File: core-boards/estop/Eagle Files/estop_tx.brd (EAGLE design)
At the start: 76.2 x 50.8 mm, 29 parts, among them J1 RFM95W-3072, J2 JST-XH-02-PIN-ROUND-PAD, J3 JST-XH-02-PIN-ROUND-PAD, J4 JST-XH-02-PIN-ROUND-PAD, J5 JST-XH-02-PIN-ROUND-PAD, J6 B2PS-VH(LF)(SN), U1 R-78E5.0-1.0CONV_R-78E5.0-1.0, U2 TXB0106PWR, U4 ATMEGA328P-AUR

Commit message: estop tx design review
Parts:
- added D4: Green, SparkFun-LED:LED-0603
- added R7: 10k, rcl:R0603
- added U$1: (no value), RoboJackets-Aesthetics:ROBOBUZZ_1.0X
- C6: device resistor:C0603 -> rcl:C0603
- R2: value 10k -> 1k
- R3: value 60k -> 10k
- R4, R5, R6: device resistor:R0603 -> rcl:R0603
- moved R3 46.2 mm to (53.0, 38.0), turned to 90 degrees
- moved R2 33.1 mm to (39.0, 7.00), turned to 180 degrees
- moved J5 29.5 mm to (31.6, 2.58), turned to 0 degrees
- moved J4 24.9 mm to (21.5, 2.63), turned to 0 degrees
- moved C5 10.4 mm to (20.9, 22.1), turned to 90 degrees
- moved C8 10.0 mm to (20.4, 8.47), turned to 270 degrees
- moved R4 2.30 mm to (39.0, 11.0), turned to 180 degrees
- moved J3 2.24 mm to (11.2, 2.56)
- moved D1 2.22 mm to (44.0, 11.0)
- moved R6 1.91 mm to (39.0, 15.0), turned to 180 degrees
- moved C4 1.89 mm to (59.0, 34.0)
- moved D3 1.82 mm to (44.0, 15.0)
- moved R5 1.68 mm to (39.0, 19.0), turned to 180 degrees
- moved D2 1.58 mm to (44.0, 19.0)
- moved C3 1.46 mm to (45.0, 30.0), turned to 90 degrees
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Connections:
- new net BUTTON_LED_CONN: J5.1, U2.3
- new net N$5: D4.C, R2.1
- new net WIRELESS_LED_CONN: J4.1, U2.1
- net !RESET: now also R3.2; no longer R2.1
- net +3V3: now also D4.A, U2.8
- net +5V: now also D1.A, R3.1; no longer D2.A, R2.2
- net BUTTON_LED: now also D3.A; no longer D1.A, J5.1, U2.3
- net CE: now also U4.14; no longer U4.7
- net GND: now also R2.2, R4.2, R5.2, R6.2, R7.2; no longer J1.9, R3.1, R4.1, R5.1, R6.1
- net N$2: now also D1.C, R4.1; no longer D2.C, R5.2
- net N$3: now also D3.C, R6.1; no longer D1.C, R4.2
- net N$4: now also D2.C, R5.1; no longer D3.C, R6.2
- net N$6: now also J1.9, R7.1; no longer R3.2, U2.8
- net WIRELESS_LED: now also D2.A; no longer D3.A, J4.1, U2.1
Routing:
- net BUTTON_LED: track 62.3 -> 43.8 mm, vias 6 -> 4
- net WIRELESS_LED: track 58.2 -> 41.2 mm
- net BUTTON_LED_CONN: track 0.00 -> 14.4 mm
- net CE: track 32.1 -> 44.7 mm
- net WIRELESS_LED_CONN: track 0.00 -> 10.6 mm
- net MISO: track 69.7 -> 64.3 mm, vias 4 -> 0
- net SCK: track 71.1 -> 67.3 mm
- net +5V: track 0.00 -> 3.42 mm
- net +3V3: track 0.00 -> 3.28 mm
- net N$5: track 0.00 -> 3.27 mm
- net MOSI: track 69.4 -> 66.2 mm, vias 0 -> 2
- net GND: track 54.6 -> 56.7 mm, vias 22 -> 23
- net N$9: track 2.47 -> 4.50 mm
- net !RESET: track 39.3 -> 37.5 mm
- net N$6: track 3.43 -> 4.53 mm
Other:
- board text added: "3V3"
- board text added: "5V"
- board text added: "BUTTON"
- board text added: "BUTTON IN"
- board text added: "E-Stop Board TX"
- board text added: "POWER"
- board text added: "POWER IN"
- board text added: "RoboJackets IGVC"
- board text added: "WIRELESS"
- board text added: "v1.2"

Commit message: almost order ready haha
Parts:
- removed J2: JST-XH-02-PIN-ROUND-PAD, IGVC-Connector:JST-XH-02-PACKAGE-ROUND-PAD
- added J7: 2-PIN_2MM-V, RoboJackets-Connectors:2MM-2-V
- added R10, R8, R9: 200, rcl:R0603
- added R11: 10k, rcl:R0603
- J3, J4, J5: value JST-XH-02-PIN-ROUND-PAD -> 2-PIN_2MM-V; device IGVC-Connector:JST-XH-02-PACKAGE-ROUND-PAD -> RoboJackets-Connectors:2MM-2-V
- moved C7 10.5 mm to (64.2, 21.7), turned to 90 degrees
- moved R1 6.30 mm to (58.5, 7.66), turned to 180 degrees
- moved J3 1.11 mm to (11.4, 3.65)
- moved J5 1.07 mm to (31.7, 3.65)
- moved J4 1.03 mm to (21.5, 3.66)
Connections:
- new net N$1: J3.1, R8.1
- new net N$10: J1.3, R11.1
- new net N$7: J4.1, R9.1
- new net N$8: J5.1, R10.1
- net +3V3: now also R8.2; no longer J3.1
- net +5V: now also R11.2
- net BUTTON_LED_CONN: now also R10.2; no longer J5.1
- net GND: now also J7.2, U2.10, U2.11, U2.12, U2.13, U2.4, U2.5, U2.6, U2.7; no longer J2.2
- net IN: now also J7.1; no longer J2.1
- net WIRELESS_LED_CONN: now also R9.2; no longer J4.1
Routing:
- net GND: track 56.7 -> 73.1 mm, vias 23 -> 24
- net BUTTON_LED_CONN: track 14.4 -> 5.13 mm
- net N$8: track 0.00 -> 8.10 mm
- net WIRELESS_LED_CONN: track 10.6 -> 3.45 mm
- net N$1: track 0.00 -> 6.08 mm
- net N$7: track 0.00 -> 5.08 mm
- net N$10: track 0.00 -> 3.97 mm
- net IN: track 27.9 -> 29.6 mm
- net WIRELESS_LED: track 41.2 -> 40.6 mm
- net BUTTON_LED: track 43.8 -> 43.2 mm

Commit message: things should be done tm
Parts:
- C1, C7: device rcl:C0603 -> rcl:C0805
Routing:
- net GND: track 73.1 -> 74.1 mm
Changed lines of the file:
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@@
 <attribute name="VALUE" x="75.946" y="14.224" size="1.27" layer="27" rot="R90" align="top-left"/>
 </element>
-<element name="C1" library="rcl" library_urn="urn:adsk.eagle:library:334" package="C0603" package3d_urn="urn:adsk.eagle:package:23616/2" value="10uF" x="65.405" y="10.922" smashed="yes" rot="R90">
+<element name="C1" library="rcl" library_urn="urn:adsk.eagle:library:334" package="C0805" package3d_urn="urn:adsk.eagle:package:23617/2" value="10uF" x="65.405" y="10.922" smashed="yes" rot="R90">
 <attribute name="NAME" x="64.77" y="10.287" size="0.5" layer="25" rot="R90"/>
-<attribute name="POPULARITY" value="37" x="65.405" y="10.922" size="1.778" layer="27" rot="R90" display="off"/>
+<attribute name="POPULARITY" value="63" x="65.405" y="10.922" size="1.778" layer="27" rot="R90" display="off"/>
 <attribute name="SPICEPREFIX" value="C" x="65.405" y="10.922" size="1.778" layer="27" rot="R90" display="off"/>
 <attribute name="VALUE" x="67.31" y="10.287" size="1.27" layer="27" rot="R90"/>
 </element>
-<element name="C7" library="rcl" library_urn="urn:adsk.eagle:library:334" package="C0603" package3d_urn="urn:adsk.eagle:package:23616/2" value="10uF" x="64.187" y="21.66" smashed="yes" rot="R90">
+<element name="C7" library="rcl" library_urn="urn:adsk.eagle:library:334" package="C0805" package3d_urn="urn:adsk.eagle:package:23617/2" value="10uF" x="64.187" y="21.66" smashed="yes" rot="R90">
 <attribute name="NAME" x="63.552" y="21.025" size="0.5" layer="25" rot="R90"/>
-<attribute name="POPULARITY" value="37" x="64.187" y="21.66" size="1.778" layer="27" rot="R90" display="off"/>
+<attribute name="POPULARITY" value="63" x="64.187" y="21.66" size="1.778" layer="27" rot="R90" display="off"/>
 <attribute name="SPICEPREFIX" value="C" x="64.187" y="21.66" size="1.778" layer="27" rot="R90" display="off"/>
 <attribute name="VALUE" x="66.092" y="21.025" size="1.27" layer="27" rot="R90"/>
@@
 </element>
 <element name="R11" library="rcl" library_urn="urn:adsk.eagle:library:334" package="R0603" package3d_urn="urn:adsk.eagle:package:23555/3" value="10k" x="31.65" y="31.27" smashed="yes" rot="R270">
-<attribute name="NAME" x="32.285" y="31.905" size="1.27" layer="25" rot="R270"/>
+<attribute name="NAME" x="32.285" y="31.905" size="0.5" layer="25" rot="R270"/>
 <attribute name="POPULARITY" value="77" x="31.65" y="31.27" size="1.778" layer="27" rot="R270" display="off"/>
 <attribute name="SPICEPREFIX" value="R" x="31.65" y="31.27" size="1.778" layer="27" rot="R270" display="off"/>
@@
 <wire x1="73.227" y1="9.227" x2="74" y2="10" width="0.4064" layer="1"/>
 <via x="74" y="10" extent="1-16" drill="0.35"/>
-<wire x1="65.405" y1="11.772" x2="65.633" y2="12" width="0.4064" layer="1"/>
-<wire x1="65.633" y1="12" x2="67" y2="12" width="0.4064" layer="1"/>
-<via x="67" y="12" extent="1-16" drill="0.35"/>
 <wire x1="73.116" y1="19.939" x2="71.061" y2="19.939" width="0.4064" layer="1"/>
 <wire x1="71.061" y1="19.939" x2="71" y2="20" width="0.4064" layer="1"/>
@@
 <wire x1="58.209" y1="44.209" x2="58" y2="44" width="0.4064" layer="1"/>
 <via x="58" y="44" extent="1-16" drill="0.35"/>
-<wire x1="64.187" y1="23.6188" x2="63.8058" y2="24" width="0.4064" layer="1"/>
-<wire x1="64.187" y1="23.6188" x2="64.187" y2="22.51" width="0.4064" layer="1"/>
-<via x="63.8058" y="24" extent="1-16" drill="0.35"/>
 <wire x1="50.752" y1="48.006" x2="52.006" y2="48.006" width="0.4064" layer="1"/>
 <wire x1="52.006" y1="48.006" x2="53" y2="49" width="0.4064" layer="1"/>
@@
 <wire x1="23.434996875" y1="12.4906" x2="23.434996875" y2="13.350003125" width="0.254" layer="1"/>
 <wire x1="23.434996875" y1="13.350003125" x2="22.785" y2="14" width="0.254" layer="1"/>
+<wire x1="65.405" y1="11.872" x2="66.128" y2="11.872" width="0.4064" layer="1"/>
+<wire x1="66.128" y1="11.872" x2="67" y2="11" width="0.4064" layer="1"/>
+<via x="67" y="11" extent="1-16" drill="0.35"/>
+<wire x1="64.187" y1="22.61" x2="62.61" y2="22.61" width="0.4064" layer="1"/>
+<wire x1="62.61" y1="22.61" x2="62" y2="22" width="0.4064" layer="1"/>
+<via x="62" y="22" extent="1-16" drill="0.35"/>
 </signal>
 <signal name="MISO">

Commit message: the ordered board :party-parrot
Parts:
- moved C8 0.22 mm to (20.6, 8.68)
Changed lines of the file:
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@@
 <attribute name="VALUE" x="22.815" y="21.461" size="1.27" layer="27" rot="R90"/>
 </element>
-<element name="C8" library="rcl" library_urn="urn:adsk.eagle:library:334" package="C0603" package3d_urn="urn:adsk.eagle:package:23616/2" value=".1uF" x="20.45" y="8.475" smashed="yes" rot="R270">
-<attribute name="NAME" x="21.085" y="9.11" size="0.5" layer="25" rot="R270"/>
-<attribute name="POPULARITY" value="37" x="20.45" y="8.475" size="1.778" layer="27" rot="R270" display="off"/>
-<attribute name="SPICEPREFIX" value="C" x="20.45" y="8.475" size="1.778" layer="27" rot="R270" display="off"/>
-<attribute name="VALUE" x="18.545" y="9.11" size="1.27" layer="27" rot="R270"/>
+<element name="C8" library="rcl" library_urn="urn:adsk.eagle:library:334" package="C0603" package3d_urn="urn:adsk.eagle:package:23616/2" value=".1uF" x="20.55" y="8.675" smashed="yes" rot="R270">
+<attribute name="NAME" x="21.185" y="9.31" size="0.5" layer="25" rot="R270"/>
+<attribute name="POPULARITY" value="37" x="20.55" y="8.675" size="1.778" layer="27" rot="R270" display="off"/>
+<attribute name="SPICEPREFIX" value="C" x="20.55" y="8.675" size="1.778" layer="27" rot="R270" display="off"/>
+<attribute name="VALUE" x="18.645" y="9.31" size="1.27" layer="27" rot="R270"/>
 </element>
 <element name="J6" library="RoboJackets-Connectors" package="B2PS-CENTERED" value="B2PS-VH(LF)(SN)" x="71.247" y="7.747" smashed="yes">
@@
 <wire x1="38.15" y1="5.15" x2="38" y2="5" width="0.4064" layer="1"/>
 <via x="38" y="5" extent="1-16" drill="0.35"/>
-<wire x1="20.45" y1="7.625" x2="21.375" y2="7.625" width="0.4064" layer="1"/>
-<wire x1="21.375" y1="7.625" x2="22" y2="7" width="0.4064" layer="1"/>
-<via x="22" y="7" extent="1-16" drill="0.35"/>
+<wire x1="20.55" y1="7.825" x2="21.825" y2="7.825" width="0.4064" layer="1"/>
+<wire x1="21.825" y1="7.825" x2="22" y2="8" width="0.4064" layer="1"/>
+<via x="22" y="8" extent="1-16" drill="0.35"/>
 <wire x1="45" y1="30.85" x2="45" y2="31.026" width="0.4064" layer="1"/>
 <wire x1="45" y1="31.026" x2="47.7335" y2="31.026" width="0.4064" layer="1"/>
@@
 <vertex x="0.21" y="0.13"/>
 </polygon>
-<wire x1="20.185" y1="12.4906" x2="20.185" y2="9.59" width="0.4064" layer="1"/>
-<wire x1="20.185" y1="9.59" x2="20.45" y2="9.325" width="0.4064" layer="1"/>
+<wire x1="20.185" y1="12.4906" x2="20.185" y2="9.89" width="0.4064" layer="1"/>
+<wire x1="20.185" y1="9.89" x2="20.55" y2="9.525" width="0.4064" layer="1"/>
 <contactref element="R8" pad="2"/>
 </signal>

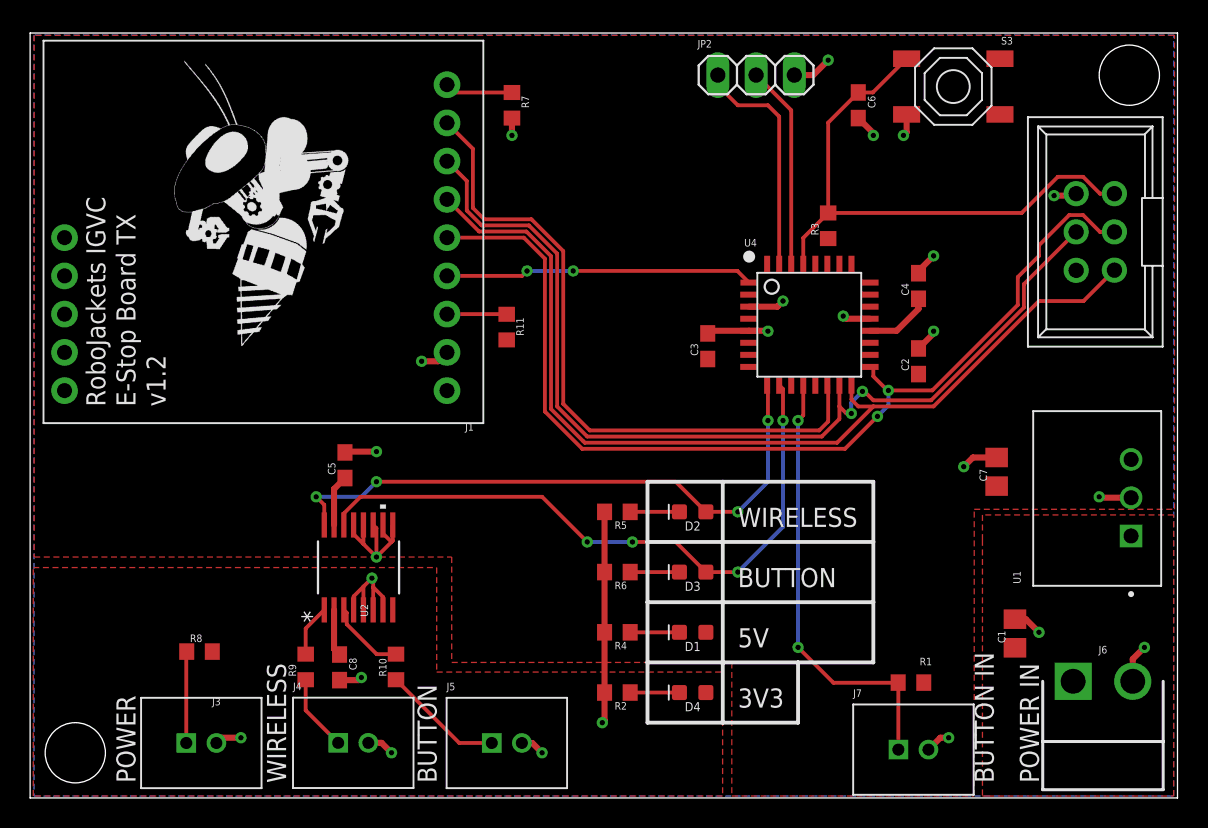
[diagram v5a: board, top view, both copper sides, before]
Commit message: Fixed estop-tx
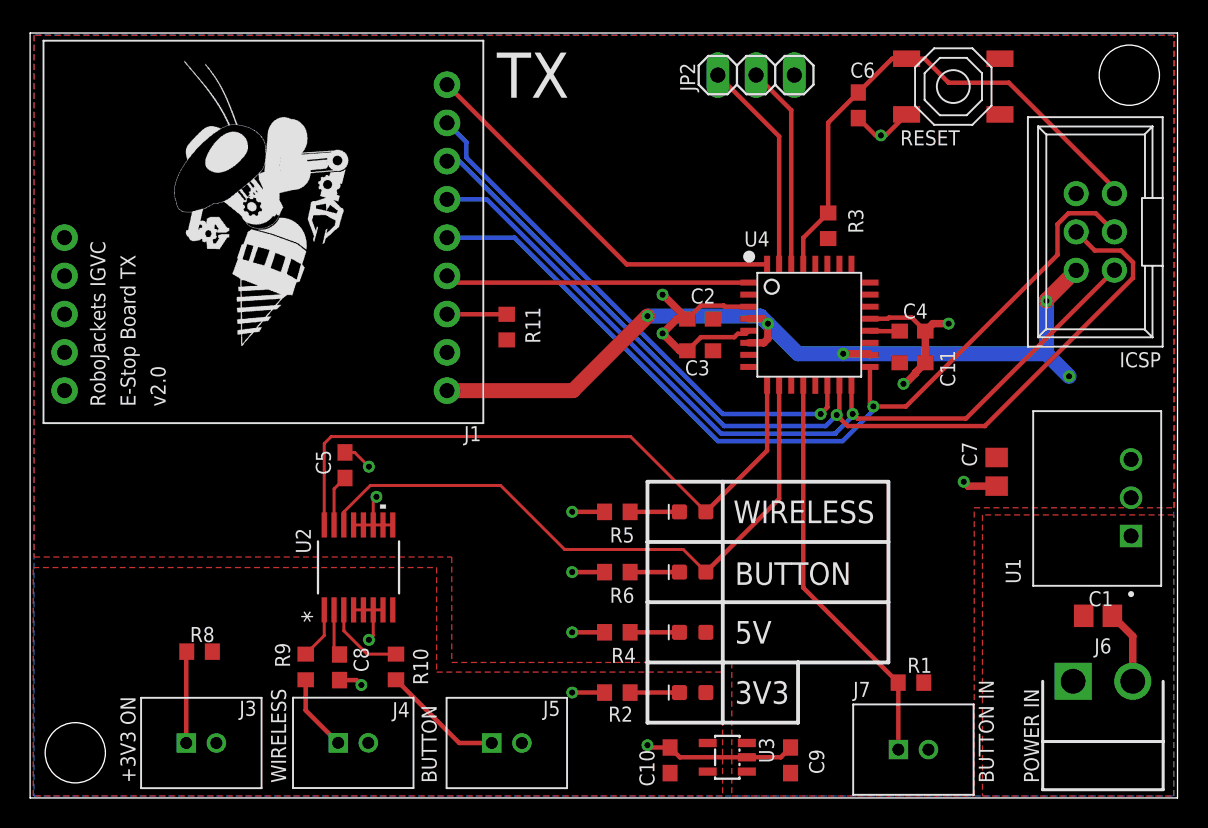
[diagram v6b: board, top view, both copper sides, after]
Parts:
- removed R7: 10k, rcl:R0603
- added C10, C9: 1uF, rcl:C0603
- added C11: 0.1uF, rcl:C0603
- added U3: MIC550X, IGVC-Regulator:SOT23-DBV
- moved C2 14.8 mm to (44.5, 31.8), turned to 180 degrees
- moved C1 5.64 mm to (70.9, 12.1), turned to 0 degrees
- moved C4 3.03 mm to (58.6, 31.0), turned to 0 degrees
- moved C3 0.58 mm to (44.5, 29.7), turned to 180 degrees
- turned C7 to 270 degrees
- renumbered PROG to ICSP, S3 to RESET
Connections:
- net IN renamed BUTTON-IN
- net N$10 renamed EN
- removed net N$6: J1.9, R7.1
- new net RADIO_RST: J1.9, U4.32
- net +3V3: now also C10.1, U3.5
- net +5V: now also C11.1, C9.1, U3.1, U3.3
- net GND: now also C10.2, C11.2, C9.2, U3.2; no longer R7.2
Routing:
- net +5V: track 3.42 -> 60.4 mm, vias 0 -> 5
- net RADIO_RST: track 0.00 -> 26.2 mm
- net CE: track 44.7 -> 35.5 mm, vias 0 -> 1
- net MISO: track 64.3 -> 57.5 mm, vias 0 -> 1
- net SCK: track 67.3 -> 60.8 mm, vias 2 -> 1
- net GND: track 73.8 -> 68.0 mm, vias 24 -> 15
- net N$6: track 4.53 -> 0.00 mm
- net BUTTON-IN: track 29.6 -> 26.8 mm, vias 2 -> 0
- net !RESET: track 37.5 -> 34.8 mm
- net N$9: track 4.50 -> 1.99 mm
- net WIRELESS_LED: track 40.6 -> 43.1 mm, vias 4 -> 0
- net TX: track 15.4 -> 14.3 mm
- net MOSI: track 66.2 -> 65.2 mm, vias 2 -> 1
- net BUTTON_LED: track 43.2 -> 42.4 mm, vias 4 -> 0
- net IRQ: track 20.5 -> 20.2 mm, vias 2 -> 0
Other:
- board text added: "+3V3 ON"
- board text added: "ICSP"
- board text added: "TX"
- board text added: "v2.0"
- board text removed: "POWER"
- board text removed: "v1.2"

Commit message: final fixes before ordering
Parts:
- added U$2, U$3: (no value), MotorBoardDev:STANDOFF-HOLE
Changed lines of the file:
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@@
 <?xml version="1.0" encoding="utf-8"?>
 <!DOCTYPE eagle SYSTEM "eagle.dtd">
-<eagle version="9.5.2">
+<eagle version="9.4.2">
 <drawing>
 <settings>
@@
 <text x="2.54" y="54.61" size="2.54" layer="27" font="vector">IGVC E-Stop Board
 v1.1</text>
-<hole x="73" y="48" drill="4"/>
-<hole x="3" y="3" drill="4"/>
 <text x="46.7" y="19" size="1.5" layer="21" font="vector" align="center-left">WIRELESS</text>
 <text x="46.8" y="14.9" size="1.5" layer="21" font="vector" align="center-left">BUTTON</text>
@@
 <text x="75.1" y="29.6" size="1" layer="21" font="vector" align="top-right">ICSP</text>
 <text x="31" y="49.5" size="3" layer="21" font="vector" align="top-left">TX</text>
+<dimension x1="0" y1="50.8" x2="0" y2="0" x3="-5" y3="25.4" textsize="1.778" layer="20"/>
 </plain>
 <attributes>
@@
 <attribute name="VALUE" x="57.965" y="26.995" size="1.27" layer="27"/>
 </element>
+<element name="U$3" library="MotorBoardDev" package="STANDOFF-HOLE" value="" x="73" y="48" smashed="yes"/>
+<element name="U$2" library="MotorBoardDev" package="STANDOFF-HOLE" value="" x="3" y="3" smashed="yes"/>
 </elements>
 <signals>
